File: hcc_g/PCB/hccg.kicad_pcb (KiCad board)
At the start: 2 copper layers, 18 x 22 mm, 26 parts, among them J1 TEST_1P, J2 TEST_1P, J3 TEST_1P, J4 TEST_1P, J5 TEST_1P, SW4 SW_PUSH, U1 MIC5353-3.3YMT-TR, U2 SAMD21G18, U4 SAMD21_MOD, Y1 Crystal_Small

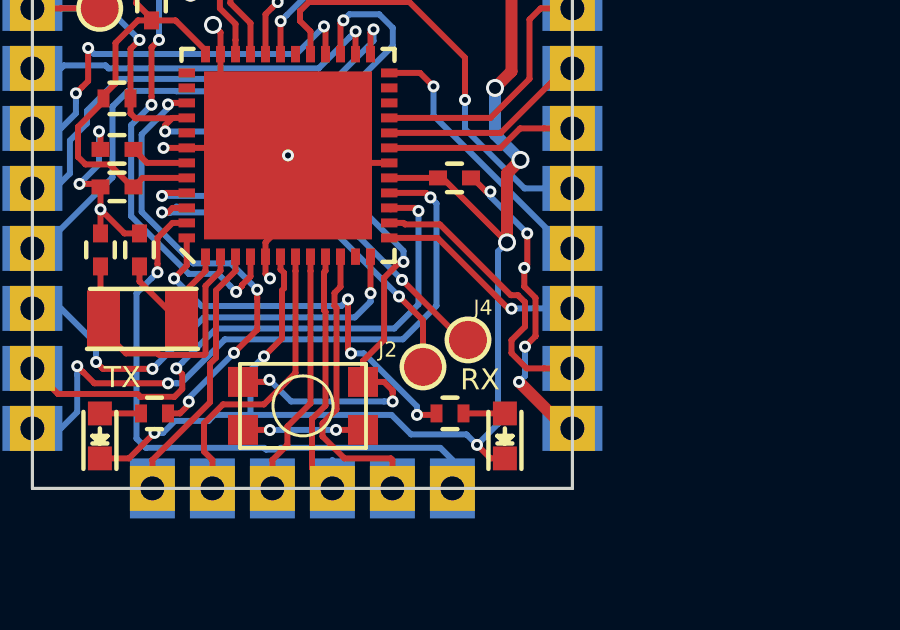
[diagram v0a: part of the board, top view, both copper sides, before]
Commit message: added demo boards
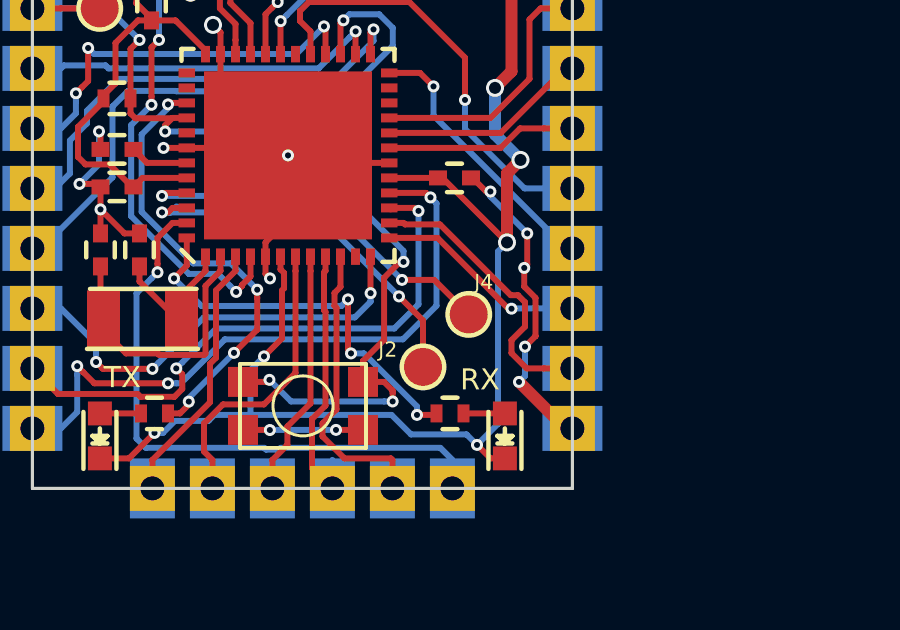
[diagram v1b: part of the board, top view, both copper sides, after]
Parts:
- moved J4 0.85 mm to (114.5, 94.2)
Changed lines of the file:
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@@
-(kicad_pcb (version 4) (host pcbnew 4.0.7)
+(kicad_pcb (version 4) (host pcbnew 4.0.4-stable)
   (general
     (links 112)
     (no_connects 0)
-    (area 99.949999 77.949999 118.050001 100.050001)
+    (area 61.42 50.05 138.435747 118.750001)
     (thickness 1.6)
     (drawings 9)
@@
   )
   (module idlehands_footprints:TESTP_1_5 (layer F.Cu)
-    (at 114.52 95.05)
+    (at 114.545 94.2)
     (fp_text reference J4 (at 0.5 -1.075) (layer F.SilkS)
       (effects (font (size 0.5 0.5) (thickness 0.125)))
@@
   (segment (start 106.250001 79.699999) (end 106.250001 83.999998) (width 0.2) (layer F.Cu) (net 7))
   (segment (start 106.250001 83.999998) (end 106.77 84.519997) (width 0.2) (layer F.Cu) (net 7))
-  (segment (start 112.32 93.05) (end 114.32 95.05) (width 0.2) (layer F.Cu) (net 8))
-  (segment (start 114.32 95.05) (end 114.52 95.05) (width 0.2) (layer F.Cu) (net 8))
+  (segment (start 112.32 93.05) (end 113.395 93.05) (width 0.2) (layer F.Cu) (net 8))
+  (segment (start 113.395 93.05) (end 114.545 94.2) (width 0.2) (layer F.Cu) (net 8))
   (segment (start 104.32 90.25) (end 109.52 90.25) (width 0.2) (layer B.Cu) (net 8))
   (segment (start 109.52 90.25) (end 112.32 93.05) (width 0.2) (layer B.Cu) (net 8))

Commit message: added logos, changed regulator to ap2112
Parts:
- removed C6: 0.1uF, Capacitors_SMD:C_0402
- added G***: LOGO, idlehands_footprints:SH_LOGO_2P5mm, F.Cu at (114.6, 84.9)
- added G***: LOGO, idlehands_footprints:IDH_Logo_3mm, F.Cu at (109.0, 94.6)
- U1: value MIC5353-3.3YMT-TR -> AP2112K-3.3V; footprint agg:DFN-6-EP-ONSEMI -> TO_SOT_Packages_SMD:SOT-23-5
- moved C8 1.95 mm to (112.2, 83.0), turned to 270 degrees
- moved U1 0.67 mm to (109.7, 81.4)
- moved C9 0.30 mm to (107.2, 82.1)
- turned D1 to 270 degrees
- turned D2 to 270 degrees
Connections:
- D1 pad 1: +3V3 -> Net-(D1-Pad1)
- D1 pad 2: Net-(D1-Pad2) -> +3V3
- D2 pad 1: +3V3 -> Net-(D2-Pad1)
- D2 pad 2: Net-(D2-Pad2) -> +3V3
- R8 pad 2: Net-(D1-Pad2) -> Net-(D1-Pad1)
- R9 pad 2: Net-(D2-Pad2) -> Net-(D2-Pad1)
- U1 pad 4: +3V3 -> (no net)
- U1 pad 5: (no net) -> +3V3
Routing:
- net GND: track 52.9 -> 54.5 mm, vias 21 -> 22
- net Net-(D2-Pad2): track 1.38 -> 0.00 mm
- net Net-(D2-Pad1): track 0.00 -> 1.38 mm
- net Net-(D1-Pad2): track 1.37 -> 0.00 mm
- net Net-(D1-Pad1): track 0.00 -> 1.37 mm
- net Net-(C6-Pad1): track 1.28 -> 0.00 mm
- net Net-(C8-Pad1): track 10.9 -> 9.74 mm
- net +3V3: track 83.6 -> 84.4 mm
- net D6: track 14.8 -> 14.0 mm
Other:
- board text added: "HCC_MOD v01a idlehandsdev.com"
- board text removed: "bridge_mod v01p"

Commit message: small changes
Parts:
- removed the G*** at (109.0, 94.6)
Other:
- board text added: "D3"
- board text added: "D4"
